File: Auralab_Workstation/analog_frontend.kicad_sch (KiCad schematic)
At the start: 19 parts, among them J1 Conn_Coaxial, J2 TEST_SOCKET, Q1 BS170, SW1 SW_SPDT, U1 TL072, U2 MCP3201, U3 REF3033, U4 INA226

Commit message: ERC checked
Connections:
- net CURRENT_IN: now also J2.2 (Pin_2)
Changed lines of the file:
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@@
 	)
 	(junction
+		(at 52.07 74.93)
+		(diameter 0)
+		(color 0 0 0 0)
+	)
+	(junction
 		(at 133.35 82.55)
 		(diameter 0)
@@
 	)
 	(junction
+		(at 34.29 74.93)
+		(diameter 0)
+		(color 0 0 0 0)
+	)
+	(junction
 		(at 57.15 92.71)
 		(diameter 0)
@@
 	(wire
 		(pts
+			(xy 52.07 74.93) (xy 53.34 74.93)
+		)
+		(stroke
+			(width 0)
+			(type default)
+		)
+	)
+	(wire
+		(pts
 			(xy 62.23 39.37) (xy 62.23 38.1)
 		)
@@
 	(wire
 		(pts
+			(xy 50.8 74.93) (xy 52.07 74.93)
+		)
+		(stroke
+			(width 0)
+			(type default)
+		)
+	)
+	(wire
+		(pts
 			(xy 62.23 24.13) (xy 62.23 29.21)
 		)
@@
 	(wire
 		(pts
+			(xy 35.56 74.93) (xy 34.29 74.93)
+		)
+		(stroke
+			(width 0)
+			(type default)
+		)
+	)
+	(wire
+		(pts
 			(xy 125.73 91.44) (xy 133.35 91.44)
 		)
@@
 	(wire
 		(pts
+			(xy 34.29 74.93) (xy 33.02 74.93)
+		)
+		(stroke
+			(width 0)
+			(type default)
+		)
+	)
+	(wire
+		(pts
 			(xy 149.86 43.18) (xy 154.94 43.18)
 		)
@@
 	(global_label "CURRENT_IN"
 		(shape bidirectional)
-		(at 234.95 30.48 180)
+		(at 236.22 30.48 180)
 		(fields_autoplaced yes)
 		(effects
@@
 		)
 		(property "Intersheetrefs" "${INTERSHEET_REFS}"
-			(at 219.363 30.48 0)
+			(at 220.633 30.48 0)
 			(effects
 				(font
@@
 	(global_label "+Vout"
 		(shape bidirectional)
-		(at 35.56 74.93 180)
+		(at 33.02 74.93 180)
 		(fields_autoplaced yes)
 		(effects
@@
 		)
 		(property "Intersheetrefs" "${INTERSHEET_REFS}"
-			(at 25.7788 74.93 0)
+			(at 23.2388 74.93 0)
 			(effects
 				(font
@@
 	(global_label "-Vout"
 		(shape bidirectional)
-		(at 50.8 74.93 0)
+		(at 53.34 74.93 0)
 		(fields_autoplaced yes)
 		(effects
@@
 		)
 		(property "Intersheetrefs" "${INTERSHEET_REFS}"
-			(at 60.5812 74.93 0)
+			(at 63.1212 74.93 0)
 			(effects
 				(font
@@
 	)
 	(symbol
+		(lib_id "power:PWR_FLAG")
+		(at 34.29 74.93 0)
+		(unit 1)
+		(exclude_from_sim no)
+		(in_bom yes)
+		(on_board yes)
+		(dnp no)
+		(fields_autoplaced yes)
+		(property "Reference" "#FLG05"
+			(at 34.29 73.025 0)
+			(effects
+				(font
+					(size 1.27 1.27)
+				)
+				(hide yes)
+			)
+		)
+		(property "Value" "PWR_FLAG"
+			(at 34.29 69.85 0)
+			(effects
+				(font
+					(size 1.27 1.27)
+				)
+			)
+		)
+		(property "Footprint" ""
+			(at 34.29 74.93 0)
+			(effects
+				(font
+					(size 1.27 1.27)
+				)
+				(hide yes)
+			)
+		)
+		(property "Datasheet" "~"
+			(at 34.29 74.93 0)
+			(effects
+				(font
+					(size 1.27 1.27)
+				)
+				(hide yes)
+			)
+		)
+		(property "Description" "Special symbol for telling ERC where power comes from"
+			(at 34.29 74.93 0)
+			(effects
+				(font
+					(size 1.27 1.27)
+				)
+				(hide yes)
+			)
+		)
+		(pin "1"
+		)
+		(instances
+			(project ""
+				(path "/0cb921c9-5493-42a4-9366-73ecb4110608"
+					(reference "#FLG01")
+					(unit 1)
+				)
+			)
+			(project "Auralab_Workstation"
+				(path "/db223ba7-bea5-428e-a07f-3236299d6518/aff8bc46-1fc9-42ac-88c6-23b3f6eac5f1"
+					(reference "#FLG05")
+					(unit 1)
+				)
+			)
+		)
+	)
+	(symbol
 		(lib_id "power:GNDA")
 		(at 213.36 106.68 0)
@@
 	)
 	(symbol
+		(lib_id "power:PWR_FLAG")
+		(at 52.07 74.93 0)
+		(unit 1)
+		(exclude_from_sim no)
+		(in_bom yes)
+		(on_board yes)
+		(dnp no)
+		(fields_autoplaced yes)
+		(property "Reference" "#FLG06"
+			(at 52.07 73.025 0)
+			(effects
+				(font
+					(size 1.27 1.27)
+				)
+				(hide yes)
+			)
+		)
+		(property "Value" "PWR_FLAG"
+			(at 52.07 69.85 0)
+			(effects
+				(font
+					(size 1.27 1.27)
+				)
+			)
+		)
+		(property "Footprint" ""
+			(at 52.07 74.93 0)
+			(effects
+				(font
+					(size 1.27 1.27)
+				)
+				(hide yes)
+			)
+		)
+		(property "Datasheet" "~"
+			(at 52.07 74.93 0)
+			(effects
+				(font
+					(size 1.27 1.27)
+				)
+				(hide yes)
+			)
+		)
+		(property "Description" "Special symbol for telling ERC where power comes from"
+			(at 52.07 74.93 0)
+			(effects
+				(font
+					(size 1.27 1.27)
+				)
+				(hide yes)
+			)
+		)
+		(pin "1"
+		)
+		(instances
+			(project "analog_frontend"
+				(path "/0cb921c9-5493-42a4-9366-73ecb4110608"
+					(reference "#FLG02")
+					(unit 1)
+				)
+			)
+			(project "Auralab_Workstation"
+				(path "/db223ba7-bea5-428e-a07f-3236299d6518/aff8bc46-1fc9-42ac-88c6-23b3f6eac5f1"
+					(reference "#FLG06")
+					(unit 1)
+				)
+			)
+		)
+	)
+	(symbol
 		(lib_id "Device:C")
 		(at 58.42 24.13 90)
@@
 		)
 	)
+	(sheet_instances
+		(path "/"
+			(page "1")
+		)
+	)
+	(embedded_fonts no)
 )

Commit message: pcb..
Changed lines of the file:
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@@
 		(fields_autoplaced yes)
 		(property "Reference" "J1"
-			(at 31.75 29.5031 0)
+			(at 35.8774 24.13 0)
 			(effects
 				(font
 					(size 1.27 1.27)
 				)
-				(justify left)
 			)
 		)
 		(property "Value" "Conn_Coaxial"
-			(at 31.75 32.0431 0)
+			(at 35.8774 26.67 0)
 			(effects
 				(font
 					(size 1.27 1.27)
 				)
-				(justify left)
 			)
 		)

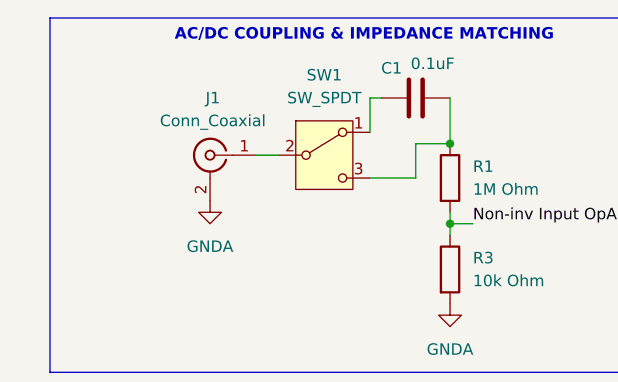
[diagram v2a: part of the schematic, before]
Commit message: removed unnecessary files
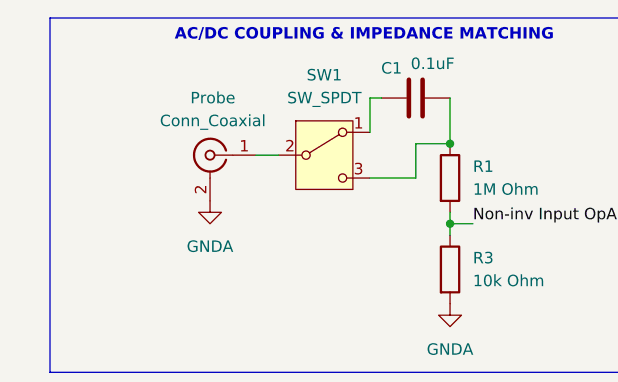
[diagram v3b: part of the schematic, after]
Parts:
- renumbered J1 to Probe
